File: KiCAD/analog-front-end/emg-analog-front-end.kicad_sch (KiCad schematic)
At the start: 42 parts, among them J1 Conn_01x03, J2 Conn_01x04_Female, J3 Conn_01x04_Female, U1 AD620, U6 AD8619ARUZ-REEL

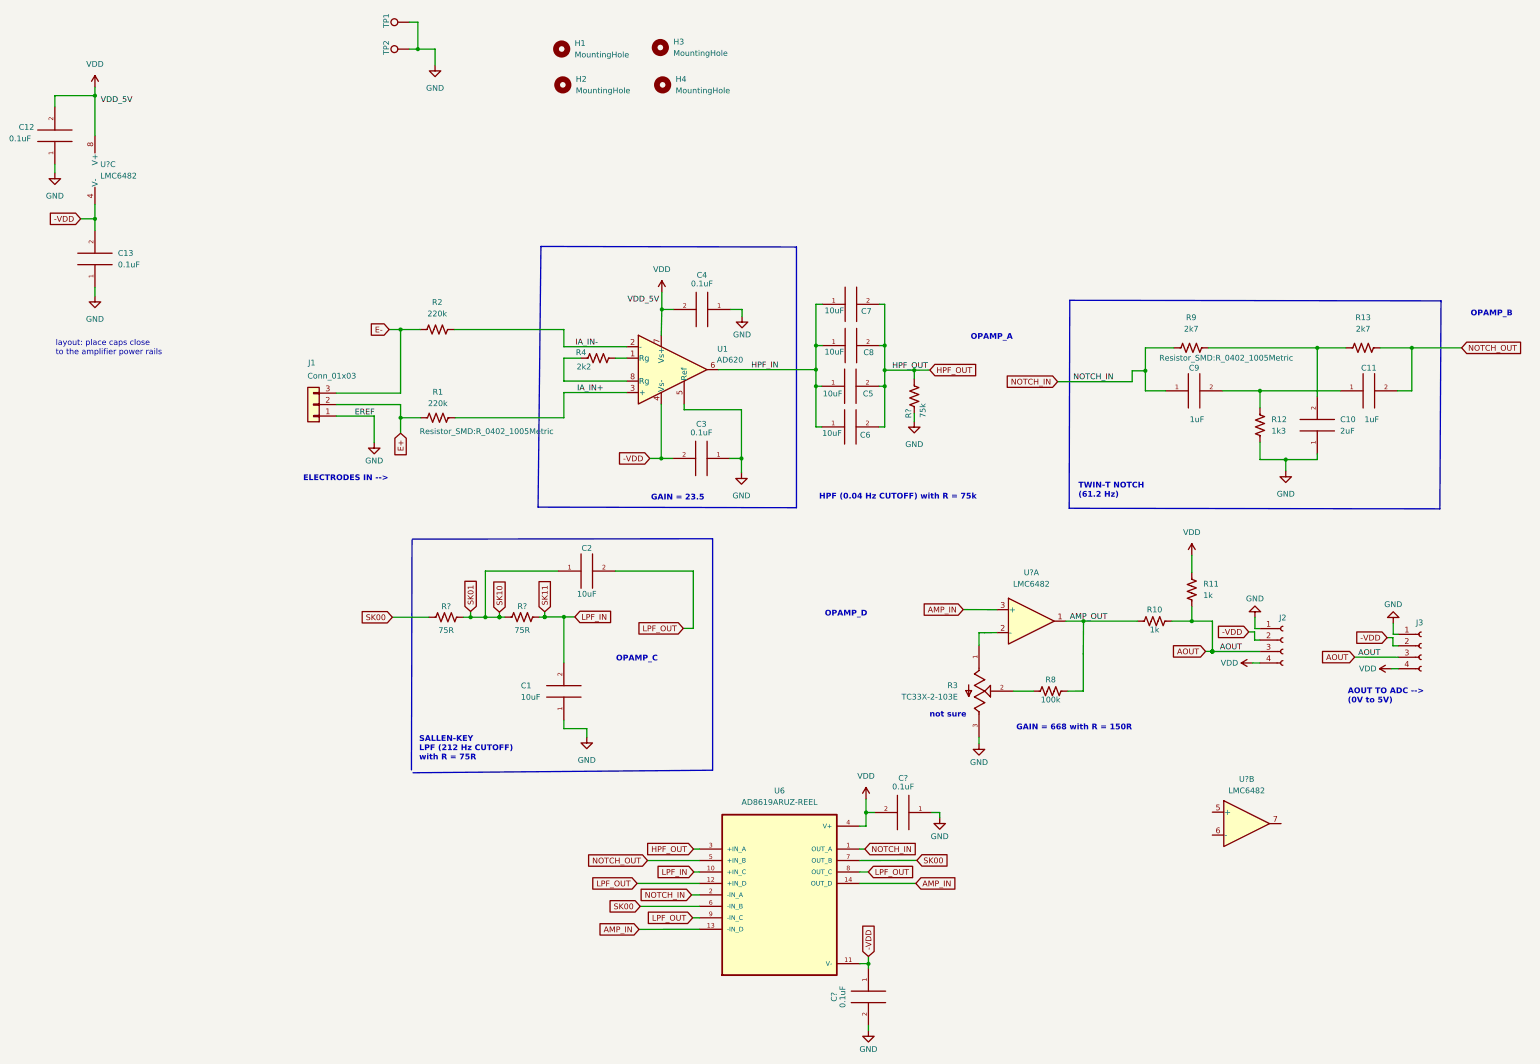
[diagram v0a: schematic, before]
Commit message: added mounting hole plates for electrodes and replaced op-amp and voltage regulator ICs
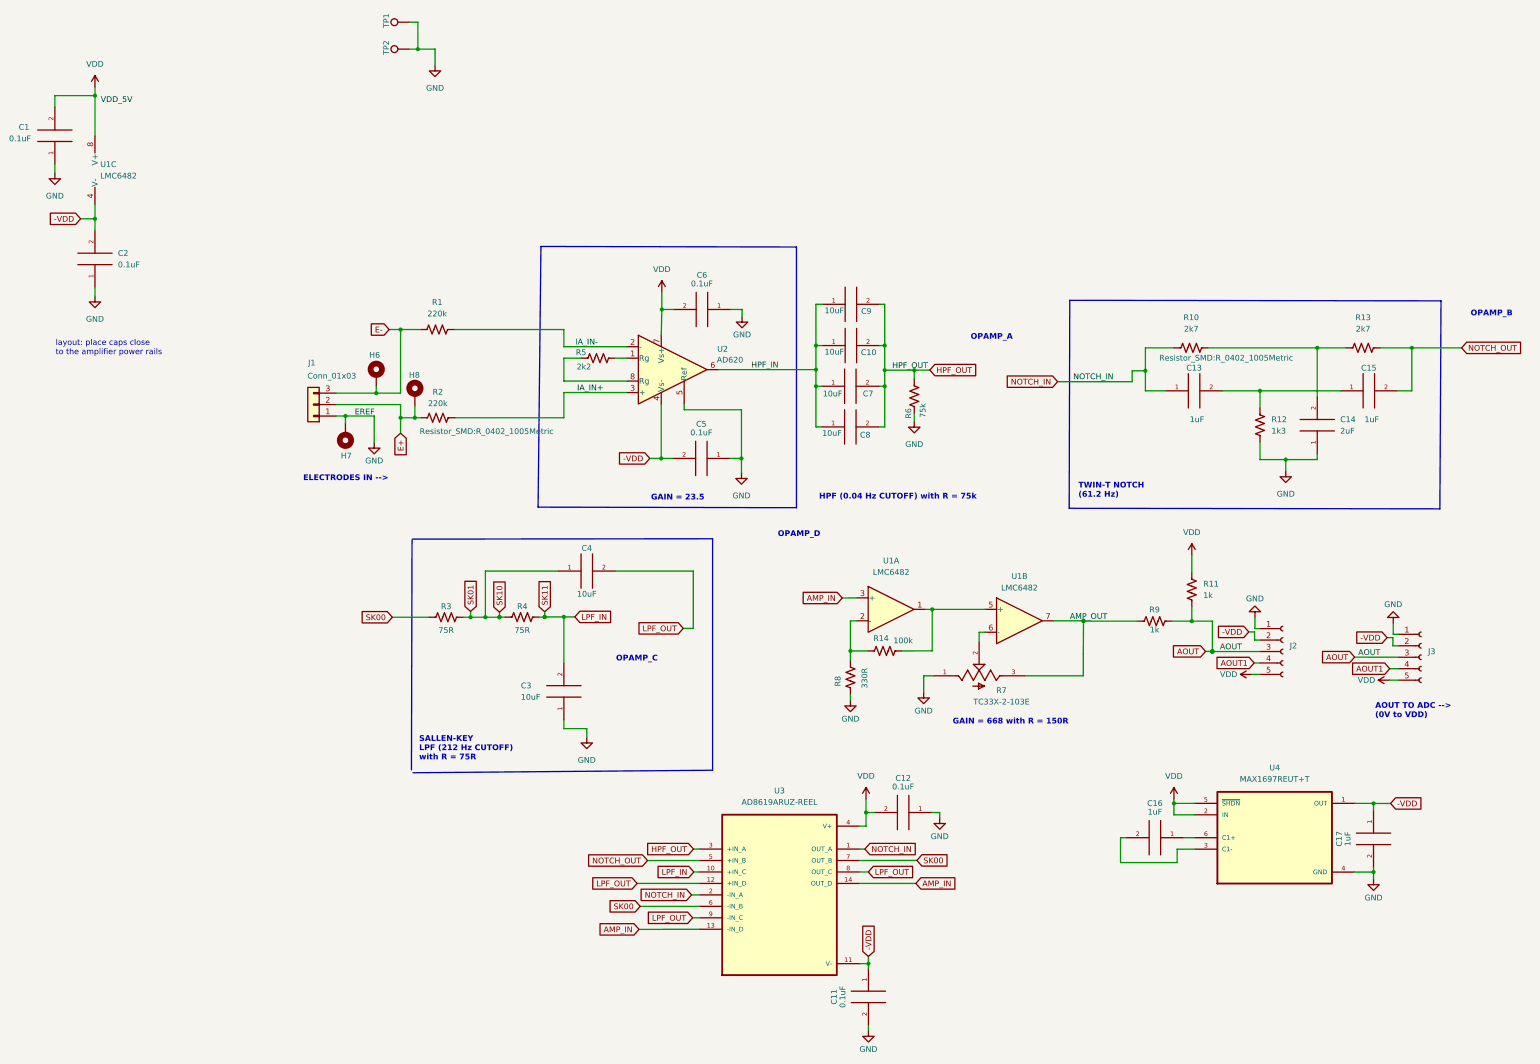
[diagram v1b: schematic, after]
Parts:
- removed H1, H2, H3, H4: MountingHole, MountingHole:MountingHole_2.2mm_M2, symbol Mechanical:MountingHole
- removed J2, J3: Conn_01x04_Female, Connector_PinHeader_1.27mm:PinHeader_1x04_P1.27mm_Vertical, symbol Connector:Conn_01x04_Female
- added C16, C17: 1uF, Capacitor_SMD:C_0402_1005Metric, symbol pspice:C
- added H6, H7, H8: MountingHole_Pad, MountingHole:MountingHole_2.2mm_M2_ISO7380_Pad, symbol Mechanical:MountingHole_Pad
- added J2, J3: Conn_01x05_Female, Connector_PinHeader_1.27mm:PinHeader_1x05_P1.27mm_Vertical, symbol Connector:Conn_01x05_Female
- added R14: 100k, Resistor_SMD:R_0402_1005Metric, symbol Device:R_US
- added U4: MAX1697REUT+T, MAX1697REUT_T:SOT95P280X145-6N, symbol MAX1697REUT_T:MAX1697REUT+T
- R8: value 100k -> 330R
- U1: renamed from U?; footprint (none) -> Package_SO:SOIC-8_3.9x4.9mm_P1.27mm
- gave numbers to parts that had none: 5
- renumbered C12 to C1, C8 to C10, C9 to C13, C10 to C14, C11 to C15, C13 to C2, C1 to C3, C2 to C4, C3 to C5, C4 to C6, C5 to C7, C6 to C8, C7 to C9, R2 to R1, R9 to R10, R1 to R2, R4 to R5, R3 to R7, R10 to R9, U1 to U2, U6 to U3
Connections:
- net -VDD: now also C11.1, C17.1, J2.2 (Pin_2), J3.2 (Pin_2), U4.1 (OUT)
- net AMP_OUT: no longer R8.1, R9.2, U1.1
- net AOUT: now also J2.3 (Pin_3), J3.3 (Pin_3)
- net E+: now also H8.1
- net E-: now also H6.1
- net GND: now also R7.1, R8.1, C17.2, H7.1, J2.1 (Pin_1), J3.1 (Pin_1), U4.4 (GND); no longer R7.3
- net VDD: now also J2.5 (Pin_5), J3.5 (Pin_5), U4.2 (IN), U4.5 (~{SHDN})
- net at U1.2 (-): now also R8.2, R14.1; no longer R7.1
- net at R7.2: now also U1.6 (-); no longer R8.2
- net at U1.5 (+): now also U1.1, R14.2
- net at U1.7: now also R7.3, R9.2
- new net: C16.2, U4.3 (C1-)
- new net: C16.1, U4.6 (C1+)
- new net AOUT1: J2.4 (Pin_4), J3.4 (Pin_4)
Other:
- note added: "AOUT TO ADC --> (0V to VDD)"
- note removed: "AOUT TO ADC --> (0V to 5V)"
- note removed: "not sure"
- moved on the sheet: R7, U1A, U1B
